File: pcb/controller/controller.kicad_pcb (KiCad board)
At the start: 2 copper layers, 100 x 40 mm, 27 parts, among them J1 Conn_01x02, J10 USB_C_Receptacle_USB2.0_16P, J2 Conn_01x02, J3 Conn_01x02, J4 Conn_01x02, J5 Conn_01x02, J6 Conn_01x02, J7 Conn_01x02, J8 RJ45, U2 AP2112K-3.3

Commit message: Final Version of new Controller Rev. 00 (Prototype)
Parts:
- added BT1: Battery_Cell, Battery:BatteryHolder_Keystone_1042_1x18650, B.Cu at (104.1, 100.0)
- added C10: 100n, Capacitor_SMD:C_0402_1005Metric, F.Cu at (127.0, 85.0)
- added C11: 100n, Capacitor_SMD:C_0402_1005Metric, F.Cu at (79.5, 109.3)
- added C12: 100n, Capacitor_SMD:C_0402_1005Metric, F.Cu at (55.2, 90.7)
- added C13: 1u, Capacitor_SMD:C_0805_2012Metric, F.Cu at (52.8, 94.5)
- added C14: 1u, Capacitor_SMD:C_0603_1608Metric, F.Cu at (60.0, 94.0)
- added C15: 2u2, Capacitor_SMD:C_0603_1608Metric, F.Cu at (60.8, 96.2)
- added C16: 1u, Capacitor_SMD:C_0805_2012Metric, F.Cu at (63.2, 95.2)
- added C17: 100u, Capacitor_SMD:CP_Elec_8x10, F.Cu at (69.2, 98.2)
- added C18: 100n, Capacitor_SMD:C_0402_1005Metric, F.Cu at (71.3, 80.0)
- added C19: 1u, Capacitor_SMD:C_0603_1608Metric, F.Cu at (72.5, 80.0)
- added C20: 1n, Capacitor_SMD:C_0402_1005Metric, F.Cu at (75.8, 80.0)
- added C21: 100u, Capacitor_SMD:CP_Elec_8x10, F.Cu at (81.5, 83.2)
- added C22: 100n, Capacitor_SMD:C_0402_1005Metric, F.Cu at (74.3, 88.0)
- added C23: 100n, Capacitor_SMD:C_0402_1005Metric, F.Cu at (86.0, 92.0)
- added C24: 1u, Capacitor_SMD:C_0805_2012Metric, F.Cu at (84.5, 91.2)
- added C25: 10u, Capacitor_SMD:C_0603_1608Metric, F.Cu at (87.8, 90.0)
- added C26: 100n, Capacitor_SMD:C_0402_1005Metric, F.Cu at (137.2, 111.2)
- added C27: 10u, Capacitor_SMD:C_0603_1608Metric, F.Cu at (142.0, 113.0)
- added C28: 10u, Capacitor_SMD:C_0603_1608Metric, F.Cu at (97.2, 95.8)
- added C29: 10u, Capacitor_SMD:C_0603_1608Metric, F.Cu at (136.5, 109.2)
- added C30: 10u, Capacitor_SMD:C_0603_1608Metric, F.Cu at (141.2, 116.2)
- added C31: 10u, Capacitor_SMD:C_0603_1608Metric, F.Cu at (135.0, 109.2)
- added C5: 100n, Capacitor_SMD:C_0402_1005Metric, F.Cu at (139.0, 85.0)
- added C6: 100n, Capacitor_SMD:C_0402_1005Metric, F.Cu at (133.0, 85.0)
- added C7: 100n, Capacitor_SMD:C_0402_1005Metric, F.Cu at (109.0, 85.0)
- added C8: 100n, Capacitor_SMD:C_0402_1005Metric, F.Cu at (115.0, 85.0)
- added C9: 100n, Capacitor_SMD:C_0402_1005Metric, F.Cu at (121.0, 85.0)
- added D1: LED, LED_SMD:LED_0603_1608Metric, F.Cu at (120.8, 107.2)
- added D10: LED, LED_SMD:LED_0603_1608Metric, F.Cu at (66.3, 107.2)
- added D11: LED, LED_SMD:LED_0603_1608Metric, F.Cu at (94.8, 88.0)
- added D2: LED, LED_SMD:LED_0603_1608Metric, F.Cu at (120.8, 105.8)
- added D3: SMAJ24A, Diode_SMD:D_SMA, F.Cu at (62.8, 113.2)
- added D4: SMAJ24A, Diode_SMD:D_SMA, F.Cu at (66.0, 86.2)
- added D5: LED, LED_SMD:LED_0603_1608Metric, F.Cu at (130.8, 123.0)
- added D6: LED, LED_SMD:LED_0603_1608Metric, F.Cu at (129.2, 123.0)
- added D7: 1N5819, Diode_SMD:D_SOD-123, F.Cu at (97.2, 91.5)
- added D8: 1N5819, Diode_SMD:D_SOD-123, F.Cu at (95.2, 109.0)
- added D9: LED, LED_SMD:LED_0603_1608Metric, F.Cu at (65.8, 90.5)
- added F1: 2.6A, Fuse:Fuse_2920_7451Metric, F.Cu at (66.0, 81.2)
- added G***: LOGO, RVNSPRK_Logo:Ravnsprk_Logo_5mm, F.Cu at (61.0, 122.0)
- added G***: LOGO, RVNSPRK_Markings:JLC-UL_1-2Layer_10mm, B.Cu at (100.2, 87.0)
- added G***: LOGO, Open-Shot-Clock:Open-Shot-Clock_QR_8mm, B.Cu at (56.2, 105.5)
- added G***: LOGO, RVNSPRK_Logo:Ravnsprk_Logo_Mask_5mm, B.Cu at (146.5, 88.8)
- added J11: JST XH, Connector_Molex:Molex_PicoBlade_53048-0210_1x02_P1.25mm_Horizontal, F.Cu at (115.6, 82.7)
- added J12: JST XH, Connector_Molex:Molex_PicoBlade_53048-0210_1x02_P1.25mm_Horizontal, F.Cu at (121.6, 82.7)
- added J13: JST XH, Connector_Molex:Molex_PicoBlade_53048-0210_1x02_P1.25mm_Horizontal, F.Cu at (127.6, 82.7)
- added J9: JST XH, Connector_Molex:Molex_PicoBlade_53048-0210_1x02_P1.25mm_Horizontal, F.Cu at (133.6, 82.7)
- added L1: 10uH, Inductor_SMD:L_Bourns_SRP1050WA, F.Cu at (58.3, 102.7)
- added L2: 2.2uH, Inductor_SMD:L_1008_2520Metric, F.Cu at (90.8, 90.8)
- added L3: 2.2uH, Inductor_SMD:L_1008_2520Metric, F.Cu at (142.0, 110.8)
- added P1: USB_C_Plug_USB2.0, Connector_USB:USB_C_Receptacle_G-Switch_GT-USB-7010ASV, F.Cu at (109.8, 122.8)
- added P2: USB_C_Plug_USB2.0, Connector_USB:USB_C_Receptacle_G-Switch_GT-USB-7010ASV, F.Cu at (123.0, 122.8)
- added Q1: 20N06, Package_SON:VSON-8_3.3x3.3mm_P0.65mm_NexFET, F.Cu at (66.5, 113.8)
- added Q2: SI2301, Package_TO_SOT_SMD:SOT-23, F.Cu at (87.0, 105.8)
- added Q3: SI2301, Package_TO_SOT_SMD:SOT-23, F.Cu at (93.5, 95.8)
- added R10: 0R, Resistor_SMD:R_0805_2012Metric, F.Cu at (52.8, 91.0)
- added R11: 10k, Resistor_SMD:R_0402_1005Metric, F.Cu at (58.5, 90.7)
- added R12: 2R2, Resistor_SMD:R_0402_1005Metric, F.Cu at (54.2, 90.7)
- added R13: 0R, Resistor_SMD:R_0805_2012Metric, F.Cu at (69.2, 106.0)
- added R14: 10k, Resistor_SMD:R_0402_1005Metric, F.Cu at (72.0, 86.0)
- added R15: 10k, Resistor_SMD:R_0402_1005Metric, F.Cu at (76.3, 86.0)
- added R16: 10k, Resistor_SMD:R_0402_1005Metric, F.Cu at (76.3, 88.0)
- added R17: 1k, Resistor_SMD:R_0402_1005Metric, F.Cu at (72.0, 88.0)
- added R18: 82k, Resistor_SMD:R_0603_1608Metric, F.Cu at (60.0, 91.0)
- added R19: 1k, Resistor_SMD:R_0402_1005Metric, F.Cu at (73.0, 86.0)
- added R20: 200k, Resistor_SMD:R_0402_1005Metric, F.Cu at (57.5, 90.7)
- added R21: 200k, Resistor_SMD:R_0402_1005Metric, F.Cu at (56.5, 90.8)
- added R22: 4k3, Resistor_SMD:R_0603_1608Metric, F.Cu at (61.5, 92.5)
- added R23: 560R, Resistor_SMD:R_0402_1005Metric, F.Cu at (73.0, 88.0)
- added R24: 0R, Resistor_SMD:R_0402_1005Metric, F.Cu at (74.3, 86.0)
- added R25: 560R, Resistor_SMD:R_0402_1005Metric, F.Cu at (74.3, 80.0)
- added R26: 1k, Resistor_SMD:R_0402_1005Metric, F.Cu at (75.3, 86.0)
- added R27: 1k, Resistor_SMD:R_0402_1005Metric, F.Cu at (75.3, 88.0)
- added R28: 0R, Resistor_SMD:R_0805_2012Metric, F.Cu at (93.2, 90.8)
- added R29: 1k, Resistor_SMD:R_0402_1005Metric, F.Cu at (130.8, 119.8)
- added R30: 1k, Resistor_SMD:R_0402_1005Metric, F.Cu at (129.2, 119.8)
- added R31: 22k, Resistor_SMD:R_0402_1005Metric, F.Cu at (85.0, 94.0)
- added R32: 200k, Resistor_SMD:R_0402_1005Metric, F.Cu at (90.5, 93.5)
- added R33: 10k, Resistor_SMD:R_0402_1005Metric, F.Cu at (86.0, 94.0)
- added R34: 0R, Resistor_SMD:R_0402_1005Metric, F.Cu at (88.0, 94.5)
- added R35: 47k, Resistor_SMD:R_0402_1005Metric, F.Cu at (90.5, 94.5)
- added R36: 200k, Resistor_SMD:R_0402_1005Metric, F.Cu at (96.0, 95.8)
- added R37: 0R, Resistor_SMD:R_0805_2012Metric, F.Cu at (141.2, 118.2)
- added R38: 10k, Resistor_SMD:R_0402_1005Metric, F.Cu at (126.5, 99.8)
- added R39: 22k, Resistor_SMD:R_0402_1005Metric, F.Cu at (68.2, 90.5)
- added R40: 10k, Resistor_SMD:R_0402_1005Metric, F.Cu at (66.2, 104.5)
- added R41: 1k, Resistor_SMD:R_0402_1005Metric, F.Cu at (92.2, 88.0)
- added R42: 22k, Resistor_SMD:R_0402_1005Metric, F.Cu at (138.2, 118.3)
- added R43: 1k, Resistor_SMD:R_0402_1005Metric, F.Cu at (133.0, 115.8)
- added R44: 1k, Resistor_SMD:R_0402_1005Metric, F.Cu at (136.2, 118.3)
- added R45: 470R, Resistor_SMD:R_0402_1005Metric, F.Cu at (135.2, 118.2)
- added R46: 470R, Resistor_SMD:R_0402_1005Metric, F.Cu at (137.2, 118.3)
- added R7: 1k, Resistor_SMD:R_0402_1005Metric, F.Cu at (106.5, 95.5)
- added R8: 200k, Resistor_SMD:R_0402_1005Metric, F.Cu at (89.2, 105.8)
- added R9: 120R, Resistor_SMD:R_0805_2012Metric, F.Cu at (76.0, 113.3)
- added REF**: OpenShotClock, RVNSPRK_Logo:OpenShotClock, B.Cu at (57.0, 89.5)
- added REF**: OSHW-Logo2_9.8x8mm_SilkScreen, Symbol:OSHW-Logo2_9.8x8mm_SilkScreen, B.Cu at (132.0, 114.8)
- added REF**: KiCad-Logo2_6mm_SilkScreen, Symbol:KiCad-Logo2_6mm_SilkScreen, B.Cu at (119.3, 113.8)
- added SW1: SW_4x3mm, RVNSPRK_Switch:SW_Push_4x3mm, F.Cu at (121.2, 98.8)
- added SW2: SW_4x3mm, RVNSPRK_Switch:SW_Push_4x3mm, F.Cu at (104.0, 94.2)
- added SW3: SW_4x3mm, RVNSPRK_Switch:SW_Push_4x3mm, F.Cu at (110.0, 91.5)
- added SW4: SW_4x3mm, RVNSPRK_Switch:SW_Push_4x3mm, F.Cu at (113.8, 91.5)
- added SW5: SW_4x3mm, RVNSPRK_Switch:SW_Push_4x3mm, F.Cu at (117.5, 91.5)
- added SW6: SW_4x3mm, RVNSPRK_Switch:SW_Push_4x3mm, F.Cu at (121.2, 91.5)
- added SW7: SW_4x3mm, RVNSPRK_Switch:SW_Push_4x3mm, F.Cu at (125.0, 91.5)
- added SW8: SW_SPDT_312, Button_Switch_THT:SW_CuK_OS102011MA1QN1_SPDT_Angled, F.Cu at (135.3, 122.0)
- added TH1: NTC, Resistor_SMD:R_0402_1005Metric, F.Cu at (126.5, 98.5)
- added U*1: BQ25606, Package_DFN_QFN:VQFN-24-1EP_4x4mm_P0.5mm_EP2.5x2.5mm_ThermalVias, F.Cu at (136.8, 114.5)
- added U3: E220-400M22S, RVNSPRK_Modules:E220-400M22S, F.Cu at (139.2, 95.5)
- added U4: SIC438BED-T1-GE3, Package_DFN_QFN:Vishay_PowerPAK_MLP44-24L_ThermalVias, F.Cu at (56.5, 94.5)
- added U5: TPS259474x, RVNSPRK_Packages:RPW0010A_VQFN-HR-10, F.Cu at (75.0, 83.0)
- added U6: TPS629206, Package_TO_SOT_SMD:SOT-583-8, F.Cu at (88.0, 92.5)
- C1, C2, C3, C4: value C -> 100n; footprint Capacitor_SMD:C_0805_2012Metric_Pad1.18x1.45mm_HandSolder -> Capacitor_SMD:C_0402_1005Metric; moved to F.Cu
- H1, H2, H3, H4: value MountingHole -> M3; footprint MountingHole:MountingHole_3mm -> MountingHole:MountingHole_3.2mm_M3
- J1, J4: value Conn_01x02 -> Term 3.5mm; footprint Connector_JST:JST_XH_B2B-XH-AM_1x02_P2.50mm_Vertical -> Connector_Phoenix_MC:PhoenixContact_MC_1,5_2-G-3.5_1x02_P3.50mm_Horizontal; moved to F.Cu
- J10: value USB_C_Receptacle_USB2.0_16P -> JST XH; footprint Connector_USB:USB_C_Receptacle_GCT_USB4105-xx-A_16P_TopMnt_Horizontal -> Connector_Molex:Molex_PicoBlade_53048-0210_1x02_P1.25mm_Horizontal; moved to F.Cu
- J2, J3: value Conn_01x02 -> RJ45; footprint Connector_JST:JST_XH_B2B-XH-AM_1x02_P2.50mm_Vertical -> Connector_RJ:RJ45_Amphenol_RJHSE5380
- J5: value Conn_01x02 -> OLED 0.96" (I2C); footprint Connector_JST:JST_XH_B2B-XH-AM_1x02_P2.50mm_Vertical -> Connector_PinSocket_2.54mm:PinSocket_1x04_P2.54mm_Vertical; moved to F.Cu
- J6, J7: value Conn_01x02 -> JST XH; footprint Connector_JST:JST_XH_B2B-XH-AM_1x02_P2.50mm_Vertical -> Connector_Molex:Molex_PicoBlade_53048-0210_1x02_P1.25mm_Horizontal; moved to F.Cu
- J8: value RJ45 -> JST XH; footprint RJ45:RJ45_Amphenol_54602-x08_Horizontal -> Connector_Molex:Molex_PicoBlade_53048-0210_1x02_P1.25mm_Horizontal; moved to F.Cu
- JP1: value SolderJumper_2_Bridged -> SolderJumper_3_Open; footprint Jumper:SolderJumper-2_P1.3mm_Bridged_RoundedPad1.0x1.5mm -> Jumper:SolderJumper-3_P1.3mm_Open_RoundedPad1.0x1.5mm_NumberLabels; moved to F.Cu
- JP2: value SolderJumper_2_Open -> SolderJumper_3_Open; footprint Jumper:SolderJumper-2_P1.3mm_Open_RoundedPad1.0x1.5mm -> Jumper:SolderJumper-3_P1.3mm_Open_RoundedPad1.0x1.5mm_NumberLabels; moved to F.Cu
- R1, R2, R3, R4: value 10k -> 1k; footprint Resistor_SMD:R_0805_2012Metric_Pad1.20x1.40mm_HandSolder -> Resistor_SMD:R_0402_1005Metric; moved to F.Cu
- R5, R6: value 10k -> 4k3; footprint Resistor_SMD:R_0805_2012Metric_Pad1.20x1.40mm_HandSolder -> Resistor_SMD:R_0402_1005Metric; moved to F.Cu
- U1: value ~ -> ESP32-S3-MINI-1; footprint Heltec_WiFi_LoRa_V3:Heltec_WiFi_LoRa_V3 -> Espressif:ESP32-S3-MINI-1U
- U2: value AP2112K-3.3 -> SP3485EN; footprint Package_TO_SOT_SMD:SOT-23-5 -> Package_SO:SOIC-8_3.9x4.9mm_P1.27mm; moved to F.Cu
- moved H4 92.8 mm to (53.8, 121.8), turned to 90 degrees
- moved H3 88.7 mm to (146.8, 121.8), turned to 90 degrees
- moved J1 76.5 mm to (58.7, 80.6), turned to -90 degrees
- moved J3 64.8 mm to (70.7, 119.1), turned to 0 degrees
- moved R3 63.5 mm to (110.5, 116.8), turned to 180 degrees
- moved J4 60.6 mm to (58.7, 111.3), turned to -90 degrees
- moved J2 58.8 mm to (90.4, 119.1), turned to 0 degrees
- moved C1 57.2 mm to (119.0, 97.8), turned to 90 degrees
- moved R2 56.8 mm to (123.8, 105.8), turned to 180 degrees
- moved R1 53.8 mm to (123.8, 107.2), turned to 180 degrees
- moved C2 47.7 mm to (106.5, 93.2), turned to 90 degrees
- moved U2 44.8 mm to (76.0, 108.3), turned to -90 degrees
- moved C3 42.2 mm to (97.0, 85.0), turned to 180 degrees
- moved J7 36.1 mm to (103.6, 82.7), turned to 180 degrees
- moved H1 35.4 mm to (89.5, 81.5), turned to 90 degrees
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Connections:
- C1 pad 1: GND -> Net-(U1-EN)
- C1 pad 2: Net-(JP2-B) -> GND
- C2 pad 1: GND -> /BOOT
- C2 pad 2: 5V_IN -> GND
- C3 pad 1: 5V -> /BTN_1
- C4 pad 1: 3V3 -> /BTN_2
- J1 pad 1: GND -> VBUS
- J1 pad 2: GPIO42 -> GND
- J2 pad 1: GND -> /Communication/RS485.A
- J2 pad 2: GPIO39 -> /Communication/RS485.B
- J3 pad 1: GND -> /Communication/RS485.A
- J3 pad 2: GPIO38 -> /Communication/RS485.B
- J4 pad 1: GND -> +12V
- J4 pad 2: GPIO34 -> Net-(D3-A2)
- J5 pad 2: GPIO26 -> Net-(J5-Pin_2)
- J6 pad 1: GND -> /BTN_1
- J6 pad 2: GPIO20 -> GND
- J7 pad 1: GND -> /BTN_2
- J7 pad 2: 5V_IN -> GND
- J8 pad 1: unconnected-(J8-Pad1) -> /BTN_8
- J8 pad 2: unconnected-(J8-Pad2) -> GND
- JP1 pad 1: 5V -> +12V
- JP1 pad 2: 5V_IN -> Net-(JP1-C)
- JP2 pad 1: 3V3 -> Net-(JP1-C)
- JP2 pad 2: Net-(JP2-B) -> Net-(JP2-C)
- R1 pad 1: GPIO34 -> +3.3V
- R1 pad 2: 3V3 -> Net-(D1-A)
- R2 pad 1: GPIO26 -> +3.3V
- R2 pad 2: 3V3 -> Net-(D2-A)
- R3 pad 1: GPIO20 -> /VUSB
- R3 pad 2: 3V3 -> /D_P
- R4 pad 1: GPIO42 -> +3.3V
- R4 pad 2: 3V3 -> Net-(U1-EN)
- R5 pad 1: GPIO39 -> +3.3V
- R5 pad 2: 3V3 -> /I2C.SDA
- R6 pad 1: GPIO38 -> +3.3V
- R6 pad 2: 3V3 -> /I2C.SCL
- U1 pad 10: unconnected-(U1-GPIO35-Pad10) -> /BTN_4
- U1 pad 11: GPIO34 -> /BTN_5
- U1 pad 12: unconnected-(U1-GPIO33-Pad12) -> /I2C.SDA
- U1 pad 13: unconnected-(U1-GPIO47-Pad13) -> /I2C.SCL
- U1 pad 14: unconnected-(U1-GPIO48-Pad14) -> /BTN_6
- U1 pad 15: GPIO26 -> /OLED_EN
- U1 pad 16: unconnected-(U1-GPIO21-Pad16) -> /UART.TX
- U1 pad 17: GPIO20 -> /UART.RX
- U1 pad 18: unconnected-(U1-GPIO19-Pad18) -> /UART.TXEN
- U1 pad 19: GND -> /HORN
- U1 pad 2: 5V -> GND
- U1 pad 20: 3V3 -> /LED.ERR
- U1 pad 21: 3V3 -> /PWR_SHDN
- U1 pad 22: unconnected-(U1-GPIO37-Pad22) -> /CHG_STAT
- U1 pad 23: unconnected-(U1-GPIO46-Pad23) -> /D_N
- U1 pad 24: unconnected-(U1-GPIO45-Pad24) -> /D_P
- U1 pad 25: GPIO42 -> /LORA.NSS
- U1 pad 27: unconnected-(U1-GPIO40-Pad27) -> /SPI.CLK
- U1 pad 28: GPIO39 -> /SPI.MOSI
- U1 pad 29: GPIO38 -> /SPI.MISO
- U1 pad 3: unconnected-(U1-Ve-Pad3) -> +3.3V
- U1 pad 30: unconnected-(U1-GPIO1-Pad30) -> /LORA.RST
- U1 pad 31: unconnected-(U1-GPIO2-Pad31) -> /LORA.BUSY
- U1 pad 32: unconnected-(U1-GPIO3-Pad32) -> /LORA.IRQ
- U1 pad 34: TX2 -> /LED.OK
- U1 pad 35: RX2 -> unconnected-(U1-MTCK/GPIO39/CLK_OUT3/SUBSPICS1-Pad35)
- U1 pad 4: unconnected-(U1-Ve-Pad4) -> /BOOT
- U1 pad 5: unconnected-(U1-RX-Pad5) -> /V_SENSE
- U1 pad 6: unconnected-(U1-TX-Pad6) -> /I_SENSE
- U1 pad 7: unconnected-(U1-RST-Pad7) -> /BTN_1
- U1 pad 8: unconnected-(U1-GPIO0-Pad8) -> /BTN_2
- U1 pad 9: unconnected-(U1-GPIO36-Pad9) -> /BTN_3
- U2 pad 1: 5V_IN -> /UART.RX
- U2 pad 2: GND -> /UART.TXEN
- U2 pad 3: 5V_IN -> /UART.TXEN
- U2 pad 4: unconnected-(U2-NC-Pad4) -> /UART.TX
- U2 pad 5: Net-(JP2-B) -> GND
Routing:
- net VBUS: track 0.00 -> 173.8 mm, vias 0 -> 7
- net GND: track 0.00 -> 144.8 mm, vias 0 -> 94
- net 3V3: track 125.0 -> 0.00 mm, vias 2 -> 0
- net VSYS: track 0.00 -> 120.9 mm, vias 0 -> 4
- net RX2: track 72.8 -> 0.00 mm
- net TX2: track 64.3 -> 0.00 mm
- net 5V: track 58.3 -> 0.00 mm
- net /BTN_6: track 0.00 -> 48.7 mm, vias 0 -> 2
- net /HORN: track 0.00 -> 47.4 mm
- net /BTN_5: track 0.00 -> 46.3 mm, vias 0 -> 2
- net /BTN_4: track 0.00 -> 43.7 mm, vias 0 -> 2
- net /BTN_3: track 0.00 -> 42.0 mm, vias 0 -> 2
- net /CHG_STAT: track 0.00 -> 41.8 mm
- net /BTN_1: track 0.00 -> 41.6 mm, vias 0 -> 2
- net /BTN_2: track 0.00 -> 39.5 mm, vias 0 -> 2
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- added copper zone on F.Cu, net +3.3V
- added copper zone on F.Cu, net +BATT
- added copper zone on F.Cu, net /Power Supply/3V3_T
- added copper zone on F.Cu, net /VUSB
- added copper zone on F.Cu, net Net-(C26-Pad1)
- added copper zone on F.Cu, net Net-(D4-A1)
- added copper zone on F.Cu, net Net-(U*1-VAC)
- added copper zone on F.Cu, net Net-(U6-SW)
- added copper zone on F.Cu, net SW
- added copper zone on F.Cu, net VCC
- added copper zone on F.Cu, net VIN
- added copper zone on F.Cu, net VSYS
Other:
- board size 100 x 40 mm -> 100 x 47.5 mm
- board text added: "1"
- board text added: "12V"
- board text added: "2"
- board text added: "3"
- board text added: "3V3"
- board text added: "4"
- board text added: "5"
- board text added: "BOOT"
- board text added: "ERR"
- board text added: "GitHub"
- board text added: "HORN"
- board text added: "OK!"
- board text added: "Open Shot Clock Controller"
- board text added: "POWER"
- board text added: "RST"
- board text added: "Rev. 00 яαvεηsραяκ 2024"
- board text added: "VIN"
- board text removed: "+"
- board text removed: "-"
- board text removed: "2024/05"
- board text removed: "5V"
- board text removed: "GND"
- board text removed: "OpenShotClock Controller v2.1"
- board text removed: "OpenShotClock Controller v2.1 by H. Ohrdes & D. Busse"

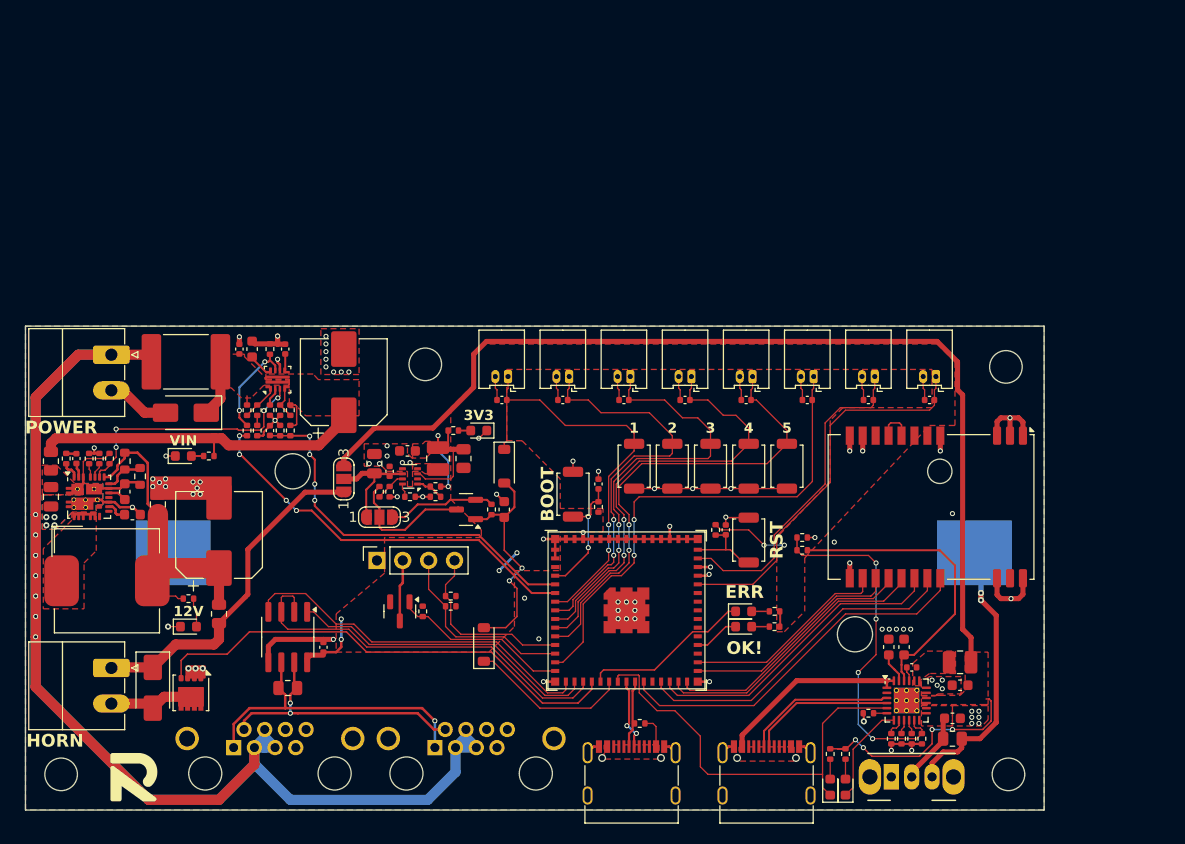
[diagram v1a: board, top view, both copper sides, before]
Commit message: Revision 01 of Controller hardware
- fixed bugs from revision 00
- changed folder structure
- added ReleaseNotes_Controller.md to keep track of changes
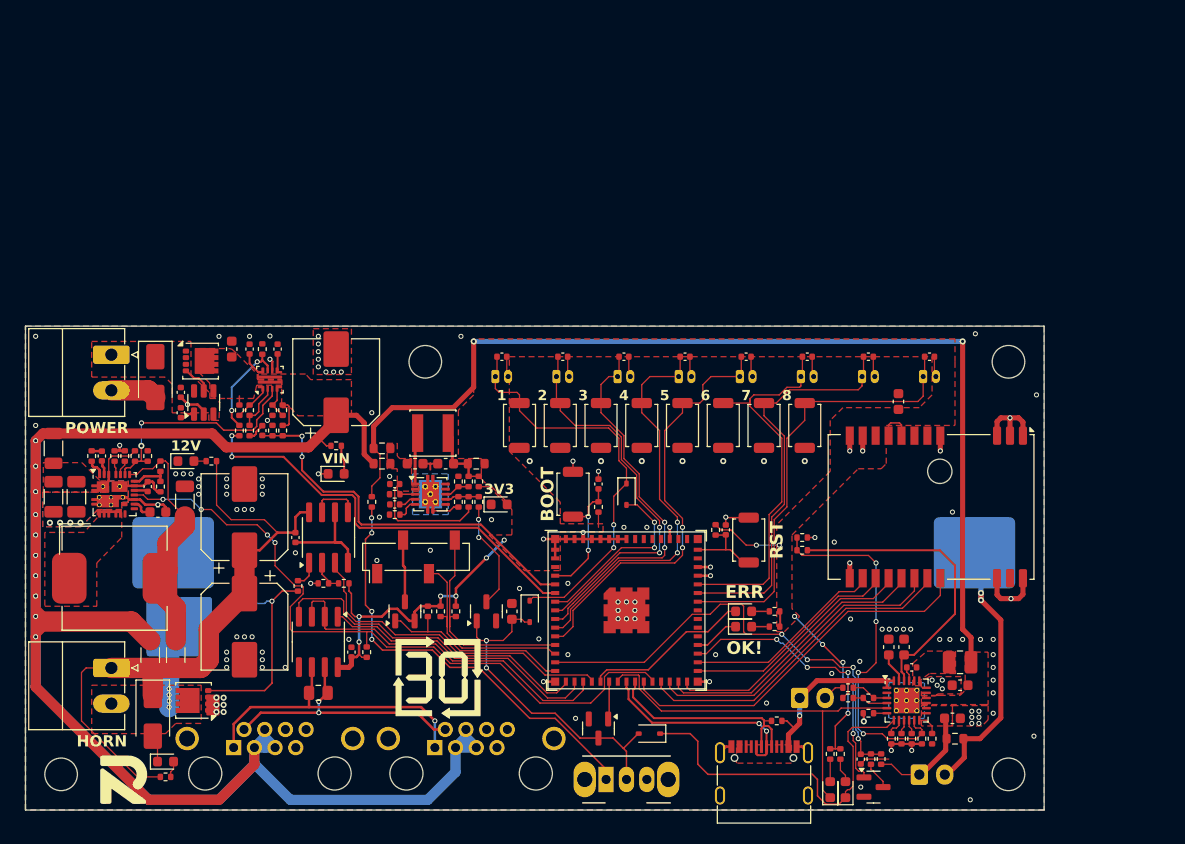
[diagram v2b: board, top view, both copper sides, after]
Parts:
- removed C23: 100n, Capacitor_SMD:C_0402_1005Metric
- removed C24: 1u, Capacitor_SMD:C_0805_2012Metric
- removed C25, C28: 10u, Capacitor_SMD:C_0603_1608Metric
- removed D4: SMAJ24A, Diode_SMD:D_SMA
- removed D7, D8: 1N5819, Diode_SMD:D_SOD-123
- removed F1: 2.6A, Fuse:Fuse_2920_7451Metric
- removed JP1, JP2: SolderJumper_3_Open, Jumper:SolderJumper-3_P1.3mm_Open_RoundedPad1.0x1.5mm_NumberLabels
- removed L2: 2.2uH, Inductor_SMD:L_1008_2520Metric
- removed P2: USB_C_Plug_USB2.0, Connector_USB:USB_C_Receptacle_G-Switch_GT-USB-7010ASV
- removed Q3: SI2301, Package_TO_SOT_SMD:SOT-23
- removed R24, R34: 0R, Resistor_SMD:R_0402_1005Metric
- removed R28: 0R, Resistor_SMD:R_0805_2012Metric
- removed R31: 22k, Resistor_SMD:R_0402_1005Metric
- removed R32, R36: 200k, Resistor_SMD:R_0402_1005Metric
- removed R33: 10k, Resistor_SMD:R_0402_1005Metric
- removed R35: 47k, Resistor_SMD:R_0402_1005Metric
- removed U6: TPS629206, Package_TO_SOT_SMD:SOT-583-8
- added C209: 100n, Capacitor_SMD:C_0402_1005Metric, F.Cu at (76.8, 98.5)
- added C302: 10u, Capacitor_SMD:C_0603_1608Metric, F.Cu at (135.9, 85.2)
- added C402: 100n, Capacitor_SMD:C_0402_1005Metric, F.Cu at (65.5, 86.2)
- added C403: 100n, Capacitor_SMD:C_0402_1005Metric, F.Cu at (65.5, 84.2)
- added C409: 10u, Capacitor_SMD:C_1206_3216Metric, F.Cu at (53.0, 94.5)
- added C415: 100u, Capacitor_SMD:CP_Elec_8x10, F.Cu at (71.8, 107.2)
- added C417: 100n, Capacitor_SMD:C_0402_1005Metric, F.Cu at (86.5, 93.2)
- added C418: 1u, Capacitor_SMD:C_0603_1608Metric, F.Cu at (88.5, 91.2)
- added C420: 100n, Capacitor_SMD:C_0402_1005Metric, F.Cu at (86.5, 95.2)
- added C421: 10u, Capacitor_SMD:C_0603_1608Metric, F.Cu at (91.5, 91.2)
- added C422: 10u, Capacitor_SMD:C_0603_1608Metric, F.Cu at (98.0, 105.8)
- added C426: 100n, Capacitor_SMD:C_0402_1005Metric, F.Cu at (132.2, 120.2)
- added D201: 1N5819WS, Diode_SMD:D_SOD-323, F.Cu at (109.2, 94.2)
- added D202: LED, LED_SMD:LED_0603_1608Metric, F.Cu at (64.0, 120.5)
- added D401: SMAJ24CA, Diode_SMD:D_SMA, F.Cu at (63.0, 82.8)
- added D404: 1N5819WS, Diode_SMD:D_SOD-323, F.Cu at (111.5, 117.8)
- added D405: 1N5819WS, Diode_SMD:D_SOD-323, F.Cu at (99.8, 105.8)
- added J101: JST XH, Connector_JST:JST_XH_B2B-XH-A_1x02_P2.50mm_Vertical, B.Cu at (126.2, 114.2)
- added J401: JST XH, Connector_JST:JST_XH_B2B-XH-A_1x02_P2.50mm_Vertical, B.Cu at (138.0, 121.8)
- added L402: 100uH, Inductor_SMD:L_Changjiang_FNR4030S, F.Cu at (90.2, 88.2)
- added Q203: Q_NMOS_GDS, Package_TO_SOT_SMD:TO-252-2, B.Cu at (66.6, 107.3)
- added Q401: DOZ35N06, Package_SON:VSON-8_3.3x3.3mm_P0.65mm_NexFET, F.Cu at (67.4, 81.2)
- added Q402: 2N7002, Package_TO_SOT_SMD:SOT-23, F.Cu at (95.5, 105.8)
- added Q403: 2N7002, Package_TO_SOT_SMD:SOT-23, F.Cu at (106.5, 117.2)
- added Q404: 2N7002, Package_TO_SOT_SMD:SOT-23, F.Cu at (133.5, 123.0)
- added R108: 4k3, Resistor_SMD:R_0402_1005Metric, F.Cu at (83.8, 109.8)
- added R202: 10k, Resistor_SMD:R_0402_1005Metric, F.Cu at (64.0, 122.0)
- added R203: 82k, Resistor_SMD:R_0402_1005Metric, F.Cu at (81.5, 103.0)
- added R204: 560R, Resistor_SMD:R_0402_1005Metric, F.Cu at (77.0, 103.2)
- added R205: 82k, Resistor_SMD:R_0402_1005Metric, F.Cu at (79.5, 103.0)
- added R401: 0R, Resistor_SMD:R_1206_3216Metric, F.Cu at (62.5, 110.0)
- added R416: 4k3, Resistor_SMD:R_0402_1005Metric, F.Cu at (62.2, 90.5)
- added R422: 0R, Resistor_SMD:R_0603_1608Metric, F.Cu at (85.2, 91.2)
- added R423: 0R, Resistor_SMD:R_0603_1608Metric, F.Cu at (85.2, 89.8)
- added R424: 0R, Resistor_SMD:R_0603_1608Metric, F.Cu at (94.5, 91.2)
- added R425: 20k, Resistor_SMD:R_0402_1005Metric, F.Cu at (93.8, 93.0)
- added R426: 1k, Resistor_SMD:R_0402_1005Metric, F.Cu at (131.0, 114.2)
- added R427: 130k, Resistor_SMD:R_0402_1005Metric, F.Cu at (84.2, 95.0)
- added R428: 200k, Resistor_SMD:R_0402_1005Metric, F.Cu at (93.8, 95.0)
- added R429: 1k, Resistor_SMD:R_0402_1005Metric, F.Cu at (133.0, 114.2)
- added R430: 200k, Resistor_SMD:R_0402_1005Metric, F.Cu at (94.8, 95.0)
- added R431: 130k, Resistor_SMD:R_0402_1005Metric, F.Cu at (92.8, 95.0)
- added R432: 0R, Resistor_SMD:R_0402_1005Metric, F.Cu at (86.5, 96.2)
- added R433: 51k, Resistor_SMD:R_0402_1005Metric, F.Cu at (86.5, 94.2)
- added R434: 13k, Resistor_SMD:R_0402_1005Metric, F.Cu at (92.8, 93.0)
- added R438: 1k, Resistor_SMD:R_0402_1005Metric, F.Cu at (131.0, 113.2)
- added R443: 10k, Resistor_SMD:R_0402_1005Metric, F.Cu at (139.2, 118.2)
- added R447: 10k, Resistor_SMD:R_0402_1005Metric, F.Cu at (133.2, 120.2)
- added R448: 4k3, Resistor_SMD:R_0402_1005Metric, F.Cu at (134.2, 120.2)
- added SW203: SW_4x3mm, RVNSPRK_Switch:SW_Push_4x3mm, F.Cu at (126.8, 87.5)
- added SW204: SW_4x3mm, RVNSPRK_Switch:SW_Push_4x3mm, F.Cu at (122.8, 87.5)
- added SW208: SW_4x3mm, RVNSPRK_Switch:SW_Push_4x3mm, F.Cu at (118.8, 87.5)
- added U201: LM358, Package_SO:SOIC-8_3.9x4.9mm_P1.27mm, F.Cu at (80.0, 98.5)
- added U403: LM74700, Package_TO_SOT_SMD:SOT-23-6, F.Cu at (67.8, 85.2)
- added U404: LM5166DRCR, Package_SON:Texas_S-PVSON-N10_ThermalVias, F.Cu at (90.0, 94.2)
- BT401: renamed from BT1; value Battery_Cell -> 18650; footprint Battery:BatteryHolder_Keystone_1042_1x18650 -> RVNSPRK_Electromechanical:BatteryHolder_SMD_1x18650
- C404: renamed from C18; value 100n -> 1u; footprint Capacitor_SMD:C_0402_1005Metric -> Capacitor_SMD:C_0603_1608Metric
- C405: renamed from C19; value 1u -> 10n; footprint Capacitor_SMD:C_0603_1608Metric -> Capacitor_SMD:C_0402_1005Metric
- C410: renamed from C13; value 1u -> 10u; footprint Capacitor_SMD:C_0805_2012Metric -> Capacitor_SMD:C_1206_3216Metric
- C411: renamed from C14; footprint Capacitor_SMD:C_0603_1608Metric -> Capacitor_SMD:C_0402_1005Metric
- C413: renamed from C16; value 1u -> 10u; footprint Capacitor_SMD:C_0805_2012Metric -> Capacitor_SMD:C_1206_3216Metric
- D203: renamed from D3; value SMAJ24A -> SS54
- J201: renamed from J5; footprint Connector_PinSocket_2.54mm:PinSocket_1x04_P2.54mm_Vertical -> Connector_PinSocket_2.54mm:PinSocket_1x04_P2.54mm_Vertical_SMD_Pin1Left
- J202: renamed from J6; value JST XH -> Picoblade; moved to B.Cu
- J203: renamed from J7; value JST XH -> Picoblade; moved to B.Cu
- J204: renamed from J8; value JST XH -> Picoblade; moved to B.Cu
- J205: renamed from J9; value JST XH -> Picoblade; moved to B.Cu
- J206: renamed from J10; value JST XH -> Picoblade; moved to B.Cu
- J207: renamed from J11; value JST XH -> Picoblade; moved to B.Cu
- J208: renamed from J12; value JST XH -> Picoblade; moved to B.Cu
- J209: renamed from J13; value JST XH -> Picoblade; moved to B.Cu
- L401: renamed from L1; value 10uH -> 6.8uH
- Q202: renamed from Q1; value 20N06 -> DOZ35N06
- R201: renamed from R8; value 200k -> 20k
- R402: renamed from R10; footprint Resistor_SMD:R_0805_2012Metric -> Resistor_SMD:R_1206_3216Metric
- R403: renamed from R11; value 10k -> 20k
- R404: renamed from R14; value 10k -> 20k
- R406: renamed from R15; value 10k -> 20k
- R407: renamed from R16; value 10k -> 20k
- R408: renamed from R13; footprint Resistor_SMD:R_0805_2012Metric -> Resistor_SMD:R_1206_3216Metric
- R409: renamed from R19; value 1k -> 2k
- R411: renamed from R18; footprint Resistor_SMD:R_0603_1608Metric -> Resistor_SMD:R_0402_1005Metric
- R412: renamed from R23; value 560R -> 0R
- R414: renamed from R26; value 1k -> 2k
- R415: renamed from R27; value 1k -> 2k
- R419: renamed from R22; footprint Resistor_SMD:R_0603_1608Metric -> Resistor_SMD:R_0402_1005Metric
- R435: renamed from R37; footprint Resistor_SMD:R_0805_2012Metric -> Resistor_SMD:R_0603_1608Metric
- R437: renamed from R42; value 22k -> 10k
- R441: renamed from R45; value 470R -> 560R
- R442: renamed from R46; value 470R -> 560R
- R444: renamed from R39; value 22k -> 20k
- REF**: moved to F.Cu
- U301: renamed from U2; value SP3485EN -> SP3485EN-L/TR
- U402: renamed from U5; value TPS259474x -> TPS259474ARPW
- U405: renamed from U*1; value BQ25606 -> BQ25616
- moved REF** 79.8 mm to (56.3, 89.6)
- moved REF** 40.5 mm to (90.5, 112.2), turned to 0 degrees
- moved SW401 28.0 mm to (107.2, 122.2)
- moved G*** 25.0 mm to (146.8, 113.8)
- moved G*** 17.2 mm to (89.0, 100.0)
- moved D407 16.3 mm to (66.0, 91.0)
- moved D406 15.1 mm to (80.8, 92.2)
- moved R445 13.7 mm to (68.5, 91.0), turned to 180 degrees
- moved R101 13.5 mm to (124.0, 116.5)
- moved P101 13.0 mm to (122.8, 122.8)
- moved R444 12.5 mm to (80.8, 89.5), turned to 0 degrees
- moved SW201 11.9 mm to (98.8, 87.5)
- moved SW202 11.7 mm to (102.8, 87.5)
- moved SW205 11.5 mm to (106.8, 87.5)
- moved SW206 11.2 mm to (110.8, 87.5)
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- renumbered C1 to C101, C2 to C102, C3 to C201, C4 to C202, C5 to C203, C6 to C204, C7 to C205, C8 to C206, C9 to C207, C10 to C208, C11 to C301, C12 to C401, C20 to C406, C21 to C407, C22 to C408, C15 to C412, C17 to C414, C26 to C416, C27 to C419, C29 to C423, C30 to C424, C31 to C425, D1 to D101, D2 to D102, D5 to D402, D6 to D403, D9 to D406, D10 to D407, D11 to D408, H1 to H101, H2 to H102, H3 to H103, H4 to H104, J1 to J102, J2 to J103, J3 to J104, J4 to J210, L3 to L403, P1 to P101, Q2 to Q201, R3 to R101, R1 to R102, R2 to R103, R4 to R104, R5 to R105, R6 to R106, R7 to R107, R9 to R301, R12 to R405, R17 to R410, R25 to R413, R20 to R417, R21 to R418, R29 to R420, R30 to R421, R38 to R436, R43 to R439, R44 to R440, R40 to R445, R41 to R446, SW1 to SW101, SW2 to SW102, SW3 to SW201, SW4 to SW202, SW5 to SW205, SW6 to SW206, SW7 to SW207, SW8 to SW401, TH1 to TH401, U1 to U101, U3 to U302, U4 to U401
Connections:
- net Net-(D5-K) renamed /Power Supply/~{BQ_PG}
- BT401 pad 1: Net-(BT1-+) -> Net-(BT401-+)
- C201 pad 1: /BTN_1 -> /BTN_1_WKUP
- C407 pad 1: VCC -> VBUS
- C413 pad 1: /Power Supply/12V_T -> Net-(U401-VOUT)
- C414 pad 1: /Power Supply/12V_T -> +12V
- J102 pad 1: VBUS -> VEXT
- J103 pad SH: (no net) -> GND
- J104 pad SH: (no net) -> GND
- J202 pad 1: /BTN_1 -> /BTN_1_WKUP
- L401 pad 2: /Power Supply/12V_T -> Net-(U401-VOUT)
- P101 pad A4: /VUSB -> /Power Supply/VUSB
- P101 pad A6: /D_P -> /USB.D+
- P101 pad A7: /D_N -> /USB.D-
- P101 pad A8: (no net) -> unconnected-(P101-SBU1-PadA8)
- P101 pad A9: /VUSB -> /Power Supply/VUSB
- P101 pad B4: /VUSB -> /Power Supply/VUSB
- P101 pad B6: (no net) -> /USB.D+
- P101 pad B7: (no net) -> /USB.D-
- P101 pad B8: (no net) -> unconnected-(P101-SBU2-PadB8)
- P101 pad B9: /VUSB -> /Power Supply/VUSB
- Q202 pad 4: /HORN -> Net-(Q202-G)
- R101 pad 1: /VUSB -> /Power Supply/VUSB
- R101 pad 2: /D_P -> /USB.D+
- R402 pad 1: VCC -> VBUS
- R406 pad 1: VCC -> VBUS
- R407 pad 1: VCC -> VBUS
- R408 pad 1: /Power Supply/12V_T -> Net-(U401-VOUT)
- R409 pad 2: Net-(R19-Pad2) -> Net-(U402-OVLO)
- R411 pad 2: /Power Supply/12V_T -> Net-(U401-VOUT)
- R412 pad 1: Net-(R19-Pad2) -> Net-(U402-OVLO)
- R420 pad 1: VSYS -> +3.3V
- R421 pad 1: VSYS -> +3.3V
- R435 pad 1: Net-(BT1-+) -> Net-(BT401-+)
- R444 pad 1: VCC -> VBUS
- R445 pad 1: /Power Supply/12V_T -> +12V
- SW201 pad 1: /BTN_1 -> /BTN_1_WKUP
- SW401 pad 1: unconnected-(SW8-A-Pad1) -> Net-(SW401-A)
- SW401 pad 2: +BATT -> Net-(D404-A)
- SW401 pad 3: Net-(BT1-+) -> GND
- U101 pad 14: /BTN_6 -> /VBAT_SENSE
- U101 pad 23: /D_N -> /USB.D-
- U101 pad 24: /D_P -> /USB.D+
- U101 pad 26: unconnected-(U1-GPIO26-Pad26) -> /12V_PG
- U101 pad 33: unconnected-(U1-SPIDQS/GPIO37/FSPIQ/SUBSPIQ-Pad33) -> /VBAT_SENSE_EN
- U101 pad 39: unconnected-(U1-U0TXD/GPIO43/CLK_OUT1-Pad39) -> /BTN_8
- U101 pad 40: unconnected-(U1-U0RXD/GPIO44/CLK_OUT2-Pad40) -> /BTN_7
- U101 pad 41: /BTN_8 -> /BTN_6
- U101 pad 44: /BTN_7 -> unconnected-(U101-GPIO46-Pad44)
- U401 pad 14: unconnected-(U4-PGOOD-Pad14) -> /12V_PG
- U401 pad 18: /Power Supply/12V_T -> Net-(U401-VOUT)
- U402 pad 2: Net-(U5-OVLO) -> Net-(U402-OVLO)
- U402 pad 6: VCC -> VBUS
- U405 pad 1: Net-(U*1-VAC) -> /Power Supply/VUSB
- U405 pad 12: unconnected-(U*1-VSET-Pad12) -> Net-(U405-VSET)
- U405 pad 24: Net-(U*1-VAC) -> /Power Supply/VUSB
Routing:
- net /12V_PG: track 0.00 -> 68.8 mm, vias 0 -> 4
- net /VBAT_SENSE: track 0.00 -> 46.5 mm, vias 0 -> 4
- net Net-(SW401-A): track 0.00 -> 42.8 mm, vias 0 -> 4
- net +3.3V: track 18.4 -> 59.4 mm, vias 6 -> 12
- net /BTN_1_WKUP: track 0.00 -> 40.2 mm, vias 0 -> 2
- net VCC: track 36.5 -> 0.00 mm
- net GND: track 144.8 -> 110.6 mm, vias 94 -> 143
- net Net-(D404-A): track 0.00 -> 33.8 mm, vias 0 -> 2
- net /Power Supply/12V_T: track 32.4 -> 0.00 mm
- net +12V: track 33.5 -> 63.7 mm
- net Net-(BT1-+): track 28.1 -> 0.00 mm, vias 2 -> 0
- net /VBAT_SENSE_EN: track 0.00 -> 27.9 mm, vias 0 -> 4
- net Net-(BT401-+): track 0.00 -> 25.9 mm, vias 0 -> 2
- net /Power Supply/~{BQ_PG}: track 10.00 -> 35.7 mm
- net VBUS: track 173.8 -> 198.8 mm, vias 7 -> 10
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- added copper zone on F.Cu, net /Power Supply/VUSB
- added copper zone on F.Cu, net Net-(D202-K)
- added copper zone on F.Cu, net Net-(U404-VIN)
- added copper zone on F.Cu, net VBUS
- added copper zone on F.Cu, net VEXT
- removed copper zone on F.Cu, net /Power Supply/3V3_T
- removed copper zone on F.Cu, net /VUSB
- removed copper zone on F.Cu, net Net-(U*1-VAC)
- removed copper zone on F.Cu, net Net-(U6-SW)
- removed copper zone on F.Cu, net VCC
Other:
- board text added: "-USB+"
- board text added: "6"
- board text added: "7"
- board text added: "8"
- board text added: "BAT on/off"
- board text added: "HORN + -"
- board text added: "POWER + -"
- board text added: "Rev. 01 яαvεηsραяκ 2025"
- board text removed: "Rev. 00 яαvεηsραяκ 2024"

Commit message: Final adjustments and BOM optimization
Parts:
- added R449: 0R, Resistor_SMD:R_0402_1005Metric, F.Cu at (123.8, 108.8)
- added R450: 0R, Resistor_SMD:R_0402_1005Metric, F.Cu at (123.8, 109.8)
- C403: value 100n -> 1u; footprint Capacitor_SMD:C_0402_1005Metric -> Capacitor_SMD:C_0603_1608Metric
- R108: value 4k3 -> 10k
- R202: value 10k -> 1k
- R203, R205: value 82k -> 20k
- moved D202 12.9 mm to (75.0, 113.8), turned to 180 degrees
- moved R202 11.7 mm to (72.2, 113.8)
- moved Q401 0.81 mm to (68.2, 81.2)
- moved U403 0.81 mm to (68.5, 85.2)
- moved C403 0.63 mm to (66.0, 84.5)
- moved C404 0.50 mm to (71.0, 80.0)
- moved C402 0.46 mm to (65.8, 86.5), turned to 0 degrees
- moved C405 0.10 mm to (72.3, 80.0)
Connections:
- D202 pad 1: Net-(D202-K) -> GND
- D203 pad 2: Net-(D202-K) -> Net-(D203-A)
- J210 pad 2: Net-(D202-K) -> Net-(D203-A)
- Q202 pad 5: Net-(D202-K) -> Net-(D203-A)
- Q203 pad 2: Net-(D202-K) -> Net-(D203-A)
- Q404 pad 1: /VBAT_SENSE_EN -> Net-(Q404-G)
- R202 pad 1: +12V -> Net-(Q202-G)
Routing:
- net /VBAT_SENSE_EN: track 27.9 -> 7.05 mm, vias 4 -> 0
- net Net-(Q404-G): track 0.00 -> 20.3 mm, vias 0 -> 4
- net +12V: track 63.7 -> 45.8 mm
- net Net-(D202-K): track 9.34 -> 0.00 mm, vias 4 -> 0
- net Net-(D203-A): track 0.00 -> 7.31 mm, vias 0 -> 4
- net GND: track 110.6 -> 113.8 mm, vias 143 -> 149
- net +3.3V: track 59.4 -> 62.4 mm
- net /LORA.NSS: track 36.7 -> 35.7 mm
- net /SPI.MOSI: track 30.4 -> 29.8 mm
- net /USB.D-: track 20.7 -> 20.1 mm
- added copper zone on F.Cu, net Net-(D203-A)
- removed copper zone on F.Cu, net Net-(D202-K)

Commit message: Update wrong values after import in JLC for production
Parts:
- C407, C414, C415: value 100u -> 150u
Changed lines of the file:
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@@
 	(title_block
 		(title "Open Shot Clock Controller")
-		(date "2025-04-09")
+		(date "2025-04-11")
 		(rev "01")
 		(company "Ravenspark")
@@
 			)
 		)
-		(property "Value" "100u"
+		(property "Value" "150u"
 			(at 0 5.2 90)
 			(layer "F.Fab")
@@
 			)
 		)
-		(property "LCSC Part #" "C5373402"
+		(property "LCSC Part #" "C2898894"
 			(at 0 0 -90)
 			(unlocked yes)
@@
 			)
 		)
-		(property "Value" "100u"
+		(property "Value" "150u"
 			(at 0 5.2 90)
 			(layer "F.Fab")
@@
 			)
 		)
-		(property "LCSC Part #" "C5373402"
+		(property "LCSC Part #" "C2898894"
 			(at 0 0 90)
 			(unlocked yes)
@@
 			)
 		)
-		(property "Value" "100u"
+		(property "Value" "150u"
 			(at 0 5.2 90)
 			(layer "F.Fab")
@@
 			)
 		)
-		(property "LCSC Part #" "C5373402"
+		(property "LCSC Part #" "C2898894"
 			(at 0 0 90)
 			(unlocked yes)
